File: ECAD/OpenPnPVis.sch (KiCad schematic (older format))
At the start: 73 parts, among them J1 USB3_B, J2 Conn_01x02, J3 Conn_01x02, Q1 CJ2305, U1 AMS1117-3.3, U10 AP2127K-2.5, U2 ﻿AR0144, U3 FT602Q, U4 AP2127K-2.8, U5 TPD4EUSB30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

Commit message: Added Courtyard to Lens mount
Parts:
- J1: footprint Image_Sensors:U235-091N-4BLRC16-4-5 -> OpenPnPVis:U235-091N-4BLRC16-4-5
- LENSMOUNT1: footprint Image_Sensors:CMT168-1122F -> OpenPnPVis:CMT168-1122F
- U2: footprint Image_Sensors:BGA-72_9x8_5.565x5.545mm -> OpenPnPVis:BGA-72_9x8_5.565x5.545mm
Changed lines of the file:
@@
 F 0 "LENSMOUNT1" H 5378 6696 50  0000 L CNN
 F 1 "CMT168-1122F" H 5378 6605 50  0000 L CNN
-F 2 "Image_Sensors:CMT168-1122F" H 5100 6200 50  0001 C CNN
+F 2 "OpenPnPVis:CMT168-1122F" H 5100 6200 50  0001 C CNN
 F 3 "http://www.optics-online.com/Detail.asp?PN=CMT168-1122F" H 5050 6400 50  0001 C CNN
 	1    5050 6650
@@
 F 0 "J1" H 1107 7067 50  0000 C CNN
 F 1 "USB3_B" H 1107 6976 50  0000 C CNN
-F 2 "Image_Sensors:U235-091N-4BLRC16-4-5" H 1200 6450 50  0001 C CNN
+F 2 "OpenPnPVis:U235-091N-4BLRC16-4-5" H 1200 6450 50  0001 C CNN
 F 3 "~" H 1200 6450 50  0001 C CNN
 F 4 "U235-091N-4BLRC16-4-5" H 1050 6350 50  0001 C CNN "MPN"
@@
 F 0 "U2" H 9400 2800 60  0000 R CNN
 F 1 "﻿AR0144" H 9650 2700 60  0000 R CNN
-F 2 "Image_Sensors:BGA-72_9x8_5.565x5.545mm" H 9300 4900 60  0001 R CNN
+F 2 "OpenPnPVis:BGA-72_9x8_5.565x5.545mm" H 9300 4900 60  0001 R CNN
 F 3 "" H 9300 4700 60  0001 R CNN
 	1    9150 4850

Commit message: Tidied Schematic and added more to readme
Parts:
- removed C15, C19, C21, C5, C7, C8: 10uF, Capacitor_SMD:C_0805_2012Metric_Pad1.15x1.40mm_HandSolder, symbol Device:C_Small
- removed C16, C17, C18, C20, C3, C4: 100nF, Capacitor_SMD:C_0402_1005Metric, symbol Device:C_Small
- removed D1, D2, D3, D4, D5: LED, LED_SMD:LED_1210_3225Metric_Pad1.42x2.65mm_HandSolder, symbol Device:LED
- removed D6, D7: LED, LED_SMD:LED_0805_2012Metric, symbol Device:LED
- removed FB2: Ferrite_Bead_Small, Resistor_SMD:R_0805_2012Metric_Pad1.15x1.40mm_HandSolder, symbol Device:Ferrite_Bead_Small
- removed H1, H2, H3, H4: M3, MountingHole:MountingHole_3.2mm_M3_Pad_Via, symbol Mechanical:MountingHole_Pad
- removed J1: USB3_B, OpenPnPVis:U235-091N-4BLRC16-4-5, symbol Connector:USB3_B
- removed Q1: CJ2305, Package_TO_SOT_SMD:SOT-23, symbol OPL_Discrete_Semiconductor:SMD-MOSFET-P-CH-8V-4.1A-CJ2305_SOT-23_
- removed R1, R17, R18, R2, R3, R4, R5: 100, Resistor_SMD:R_0805_2012Metric_Pad1.15x1.40mm_HandSolder, symbol Device:R_Small
- removed R14, R16: 0R, Resistor_SMD:R_0805_2012Metric_Pad1.15x1.40mm_HandSolder, symbol Device:R_Small
- removed TP1: TestPoint, TestPoint:TestPoint_Loop_D1.80mm_Drill1.0mm_Beaded, symbol Connector:TestPoint
- removed U1: AMS1117-3.3, Package_TO_SOT_SMD:SOT-223-3_TabPin2, symbol Regulator_Linear:AMS1117-3.3
- removed U10: AP2127K-2.5, Package_TO_SOT_SMD:SOT-23-5, symbol Regulator_Linear:AP2127K-2.5
- removed U4: AP2127K-2.8, Package_TO_SOT_SMD:SOT-23-5, symbol Regulator_Linear:AP2127K-2.8
- removed U5: TPD4EUSB30, Package_SON:USON-10_2.5x1.0mm_P0.5mm, symbol Power_Protection:TPD4EUSB30
- removed U6: AP2127K-1.2, Package_TO_SOT_SMD:SOT-23-5, symbol Regulator_Linear:AP2127K-1.2
- removed U7: ATtiny10-TS, Package_TO_SOT_SMD:SOT-23-6_Handsoldering, symbol MCU_Microchip_ATtiny:ATtiny10-TS
- removed U9: TPD2EUSB30, Package_TO_SOT_SMD:Texas_DRT-3, symbol Power_Protection:TPD2EUSB30
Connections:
- net +2V8: no longer U8.6 (~CLR), U8.7 (~PRE), U8.8 (VCC)
- new net VCC: U8.6 (~CLR), U8.7 (~PRE), U8.8 (VCC)
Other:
- note removed: "USB 3.1 INTERFACE"
- moved on the sheet: C1, C10, C11, C12, C13, C14, C2, C22, C23, C6, C9, FB1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

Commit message: Updated Crystal and LED Resistors
Updated Crystal Capacitors to 16pF and 5V series resistors for LED's to 85Ohm.
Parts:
- C1, C2: value 100nF -> 16pF
- Y1: value 30MHz -> X3S030000BA1H-U
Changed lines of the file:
@@
 P 1000 1100
 F 0 "C1" H 1092 1146 50  0000 L CNN
-F 1 "100nF" H 1092 1055 50  0000 L CNN
+F 1 "16pF" H 1092 1055 50  0000 L CNN
 F 2 "Capacitor_SMD:C_0402_1005Metric" H 1000 1100 50  0001 C CNN
 F 3 "~" H 1000 1100 50  0001 C CNN
@@
 P 1500 1100
 F 0 "C2" H 1592 1146 50  0000 L CNN
-F 1 "100nF" H 1592 1055 50  0000 L CNN
+F 1 "16pF" H 1592 1055 50  0000 L CNN
 F 2 "Capacitor_SMD:C_0402_1005Metric" H 1500 1100 50  0001 C CNN
 F 3 "~" H 1500 1100 50  0001 C CNN
@@
 P 1250 900
 F 0 "Y1" H 1250 1168 50  0000 C CNN
-F 1 "30MHz" H 1250 1077 50  0000 C CNN
+F 1 "X3S030000BA1H-U" H 1250 1077 50  0000 C CNN
 F 2 "Crystal:Crystal_SMD_3225-4Pin_3.2x2.5mm" H 1250 900 50  0001 C CNN
-F 3 "~" H 1250 900 50  0001 C CNN
+F 3 "https://datasheet.lcsc.com/szlcsc/1912111437_HELE-Harmony-Elec-X3S030000BA1H-U_C254267.pdf" H 1250 900 50  0001 C CNN
 	1    1250 900
 	-1   0    0    -1
@@
 Text GLabel 7150 4900 0    50   Input ~ 0
 FLASH_SIG
-Wire Bus Line
-	6900 2900 6900 3700
-Wire Bus Line
-	10800 5100 10800 5950
 Text GLabel 3950 6900 0    50   Input ~ 0
 LED_V+
@@
 Text GLabel 3250 5400 0    50   Input ~ 0
 USB_SSRX-
+Wire Bus Line
+	6900 2900 6900 3700
+Wire Bus Line
+	10800 5100 10800 5950
 $EndSCHEMATC

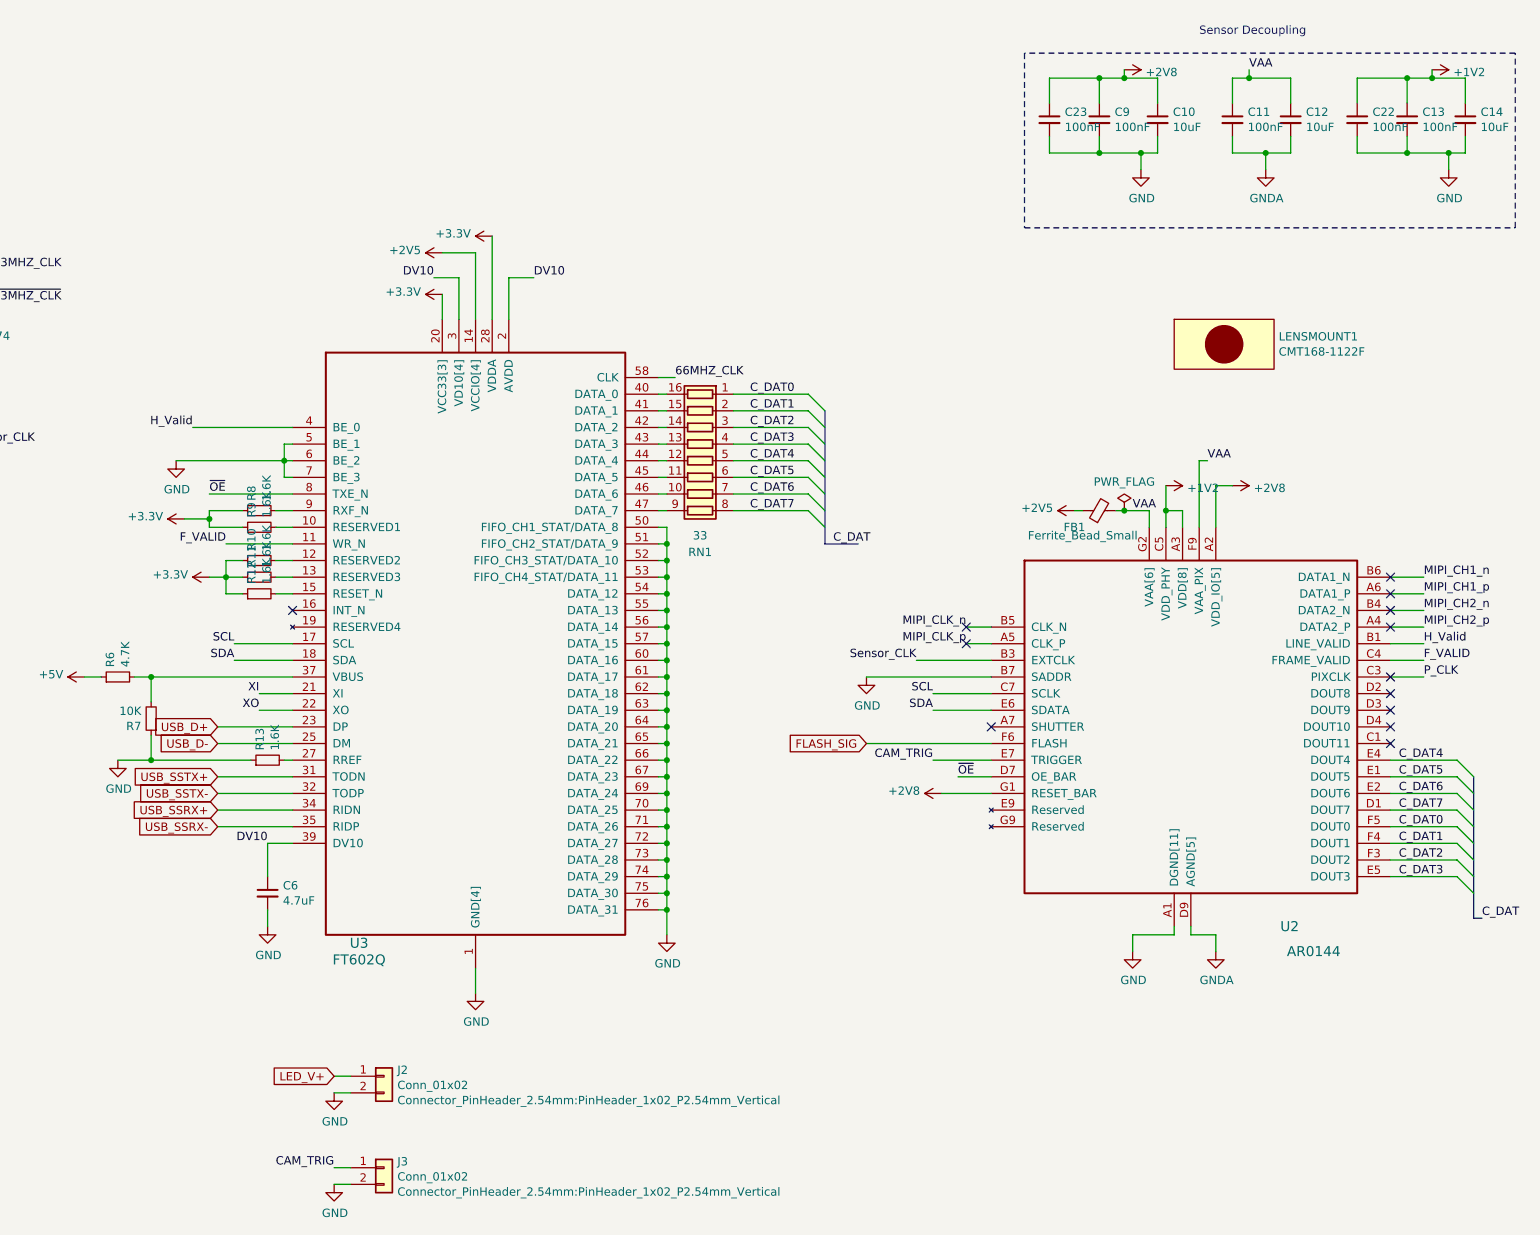
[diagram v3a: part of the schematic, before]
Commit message: Creation of Rev003
Creation of Rev003. This is a mini-sized board for easier fitment into tight spaces. The USB connector has changed to a USB Type-C. Some components have changed footprint to 0402.
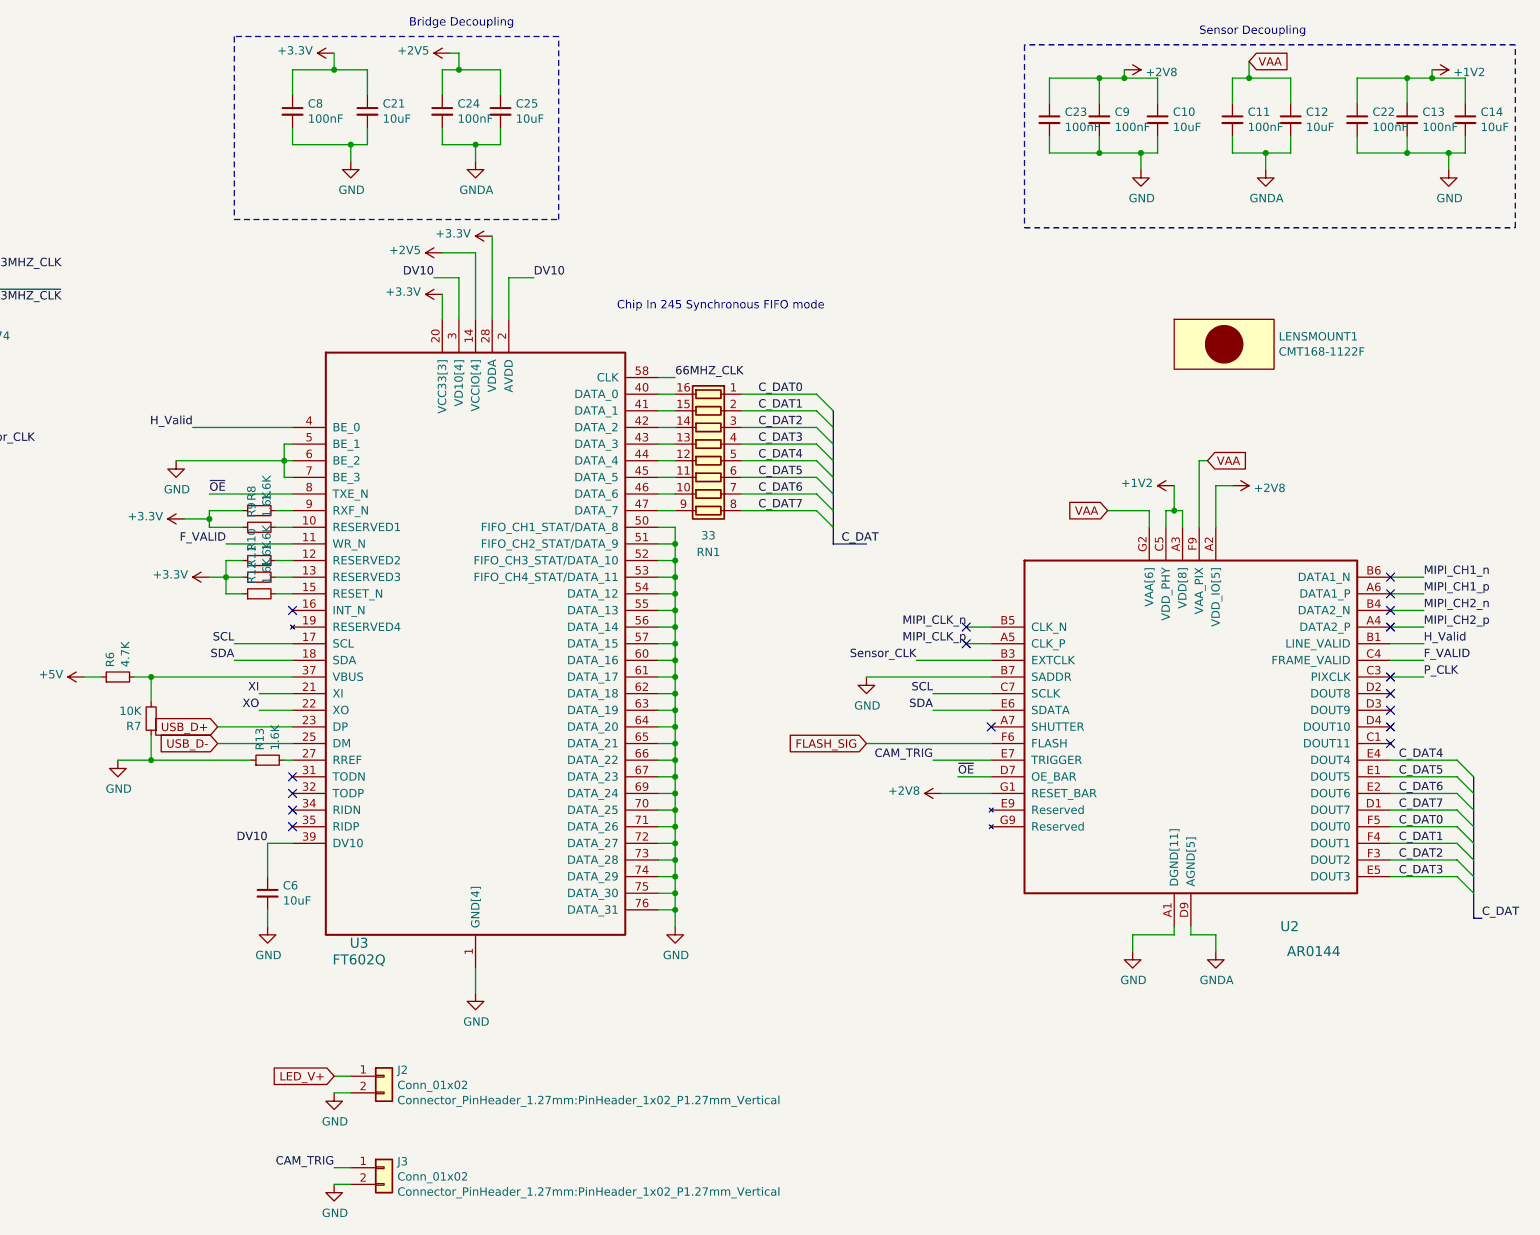
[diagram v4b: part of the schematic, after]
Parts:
- removed FB1: Ferrite_Bead_Small, Resistor_SMD:R_0805_2012Metric_Pad1.15x1.40mm_HandSolder, symbol Device:Ferrite_Bead_Small
- added C21, C25: 10uF, Capacitor_SMD:C_0805_2012Metric_Pad1.15x1.40mm_HandSolder, symbol Device:C_Small
- added C24, C8: 100nF, Capacitor_SMD:C_0402_1005Metric, symbol Device:C_Small
- C1, C2: MPN (none) -> CC0402JRNPO9BN160
- C10, C12, C14: MPN (none) -> CL21A106KOQNNNE
- C11, C13, C22, C23, C9: MPN (none) -> CC0402KRX7R7BB104
- C6: value 4.7uF -> 10uF; MPN (none) -> CL21A106KOQNNNE
- J2, J3: footprint Connector_PinHeader_2.54mm:PinHeader_1x02_P2.54mm_Vertical -> Connector_PinHeader_1.27mm:PinHeader_1x02_P1.27mm_Vertical
- LENSMOUNT1: MPN (none) -> N/A
- R10, R11, R12, R13, R8, R9: footprint Resistor_SMD:R_0805_2012Metric_Pad1.15x1.40mm_HandSolder -> Resistor_SMD:R_0402_1005Metric; MPN RC0805JR-071KL -> RC0402FR-071K5L
- R19, R20: footprint Resistor_SMD:R_0805_2012Metric_Pad1.15x1.40mm_HandSolder -> Resistor_SMD:R_0402_1005Metric; MPN RC0805FR-070RL -> RC0402FR-070RL
- R6: footprint Resistor_SMD:R_0805_2012Metric_Pad1.15x1.40mm_HandSolder -> Resistor_SMD:R_0402_1005Metric; MPN RC0805JR-074K7L -> RC0402FR-074K7L
- R7: footprint Resistor_SMD:R_0805_2012Metric_Pad1.15x1.40mm_HandSolder -> Resistor_SMD:R_0402_1005Metric; MPN RC0805JR-0710KL -> RC0402JR-0710KL
- RN1: MPN (none) -> EXB2HV330JV
- U2: MPN (none) -> AR0144
- Y1: MPN (none) -> X3S030000BA1H-U
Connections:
- net +2V5: now also C24.1, C25.1
- net +3V3: now also C21.1, C8.1
- net GND: now also C21.2, C8.2
- net GNDA: now also C24.2, C25.2
- net USB_SSRX+: no longer names the net of U3.34 (RIDN)
- net USB_SSRX-: no longer names the net of U3.35 (RIDP)
- net USB_SSTX+: no longer names the net of U3.31 (TODN)
- net USB_SSTX-: no longer names the net of U3.32 (TODP)
- no-connect marks 13 -> 17
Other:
- note added: "Bridge Decoupling"
- note added: "Chip In 245 Synchronous FIFO mode"
- moved on the sheet: RN1

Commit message: V004 Update
Added ICSP pads
Updated 74LVC2G74 footprint
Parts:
- U8: footprint Package_SO:MSOP-8_3x3mm_P0.65mm -> Package_SO:VSSOP-8_2.4x2.1mm_P0.5mm
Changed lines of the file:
@@
 F 0 "U8" H 1750 1950 50  0000 C CNN
 F 1 "74LVC2G74" H 1800 1850 50  0000 C CNN
-F 2 "Package_SO:MSOP-8_3x3mm_P0.65mm" H 1500 2150 50  0001 C CNN
+F 2 "Package_SO:VSSOP-8_2.4x2.1mm_P0.5mm" H 1500 2150 50  0001 C CNN
 F 3 "http://www.ti.com/lit/sg/scyt129e/scyt129e.pdf" H 1500 2150 50  0001 C CNN
 F 4 "74LVC2G74" H 1500 2150 50  0001 C CNN "MPN"

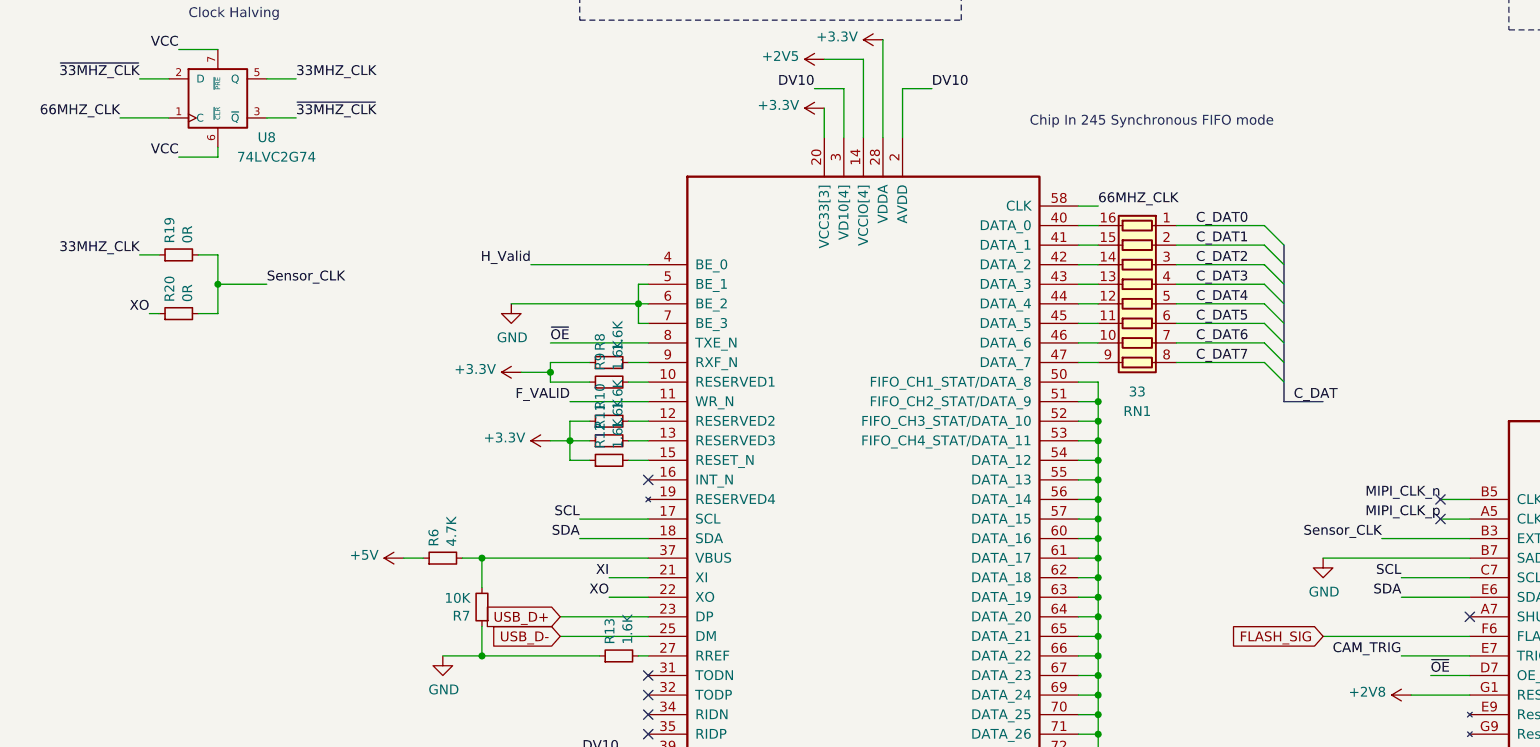
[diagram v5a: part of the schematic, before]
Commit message: V005 Release
V0005 Replaces the ATTINY10 with an ATTINY1606, It also adds a breakaway expansion I/O and programming header.

The ATTINY is now on the I2C bus, and the flip/flop reset is now tied to the ATTINY GPIO.
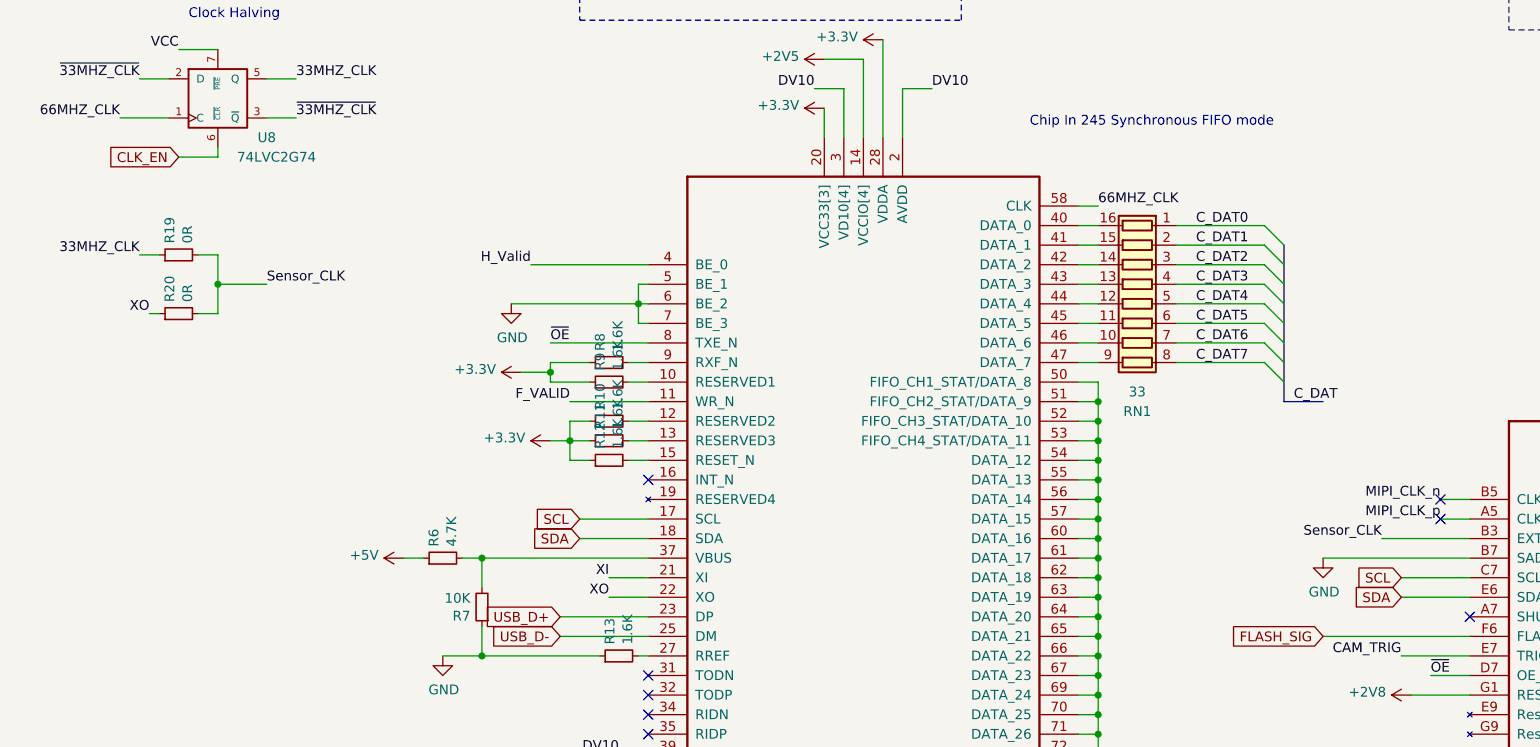
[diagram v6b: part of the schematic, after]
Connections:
- net VCC: no longer U8.6 (~CLR)
- new net CLK_EN: U8.6 (~CLR)
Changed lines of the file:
@@
 Wire Wire Line
 	3700 4300 3350 4300
-Text Label 3350 4300 2    50   ~ 0
-SCL
 Wire Wire Line
 	3700 4400 3350 4400
-Text Label 3350 4400 2    50   ~ 0
-SDA
 Wire Wire Line
 	7900 4600 7550 4600
-Text Label 7550 4600 2    50   ~ 0
-SCL
 Wire Wire Line
 	7900 4700 7550 4700
-Text Label 7550 4700 2    50   ~ 0
-SDA
 $Comp
 L Device:R_Small R10
@@
 Wire Wire Line
 	1900 2050 1750 2050
-Text Label 1300 2450 2    50   ~ 0
-VCC
 $Comp
 L 74xGxx:74LVC2G74 U8
@@
 	1    0    0    -1
 $EndComp
+Text GLabel 7550 4700 0    50   Input ~ 0
+SDA
+Text GLabel 7550 4600 0    50   Input ~ 0
+SCL
+Text GLabel 3350 4300 0    50   Input ~ 0
+SCL
+Text GLabel 3350 4400 0    50   Input ~ 0
+SDA
+Text GLabel 1300 2450 0    50   Input ~ 0
+CLK_EN
 Wire Bus Line
 	6950 2900 6950 3700
